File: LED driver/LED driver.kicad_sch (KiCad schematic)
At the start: 49 parts, among them J1 Conn_VCC, J2 Conn_LED, J3 Conn_UART, J4 Conn_01x10, P1 USB_C_Plug_USB2.0, Q1 IRFZ44NS, Q2 IRFZ44NS, Q3 IRFZ44NS, Q4 IRFZ44NS, Q5 IRFZ44NS, SW1 SW_Push, U1 ESP32-S2-WROVER-I, U2 MP2359

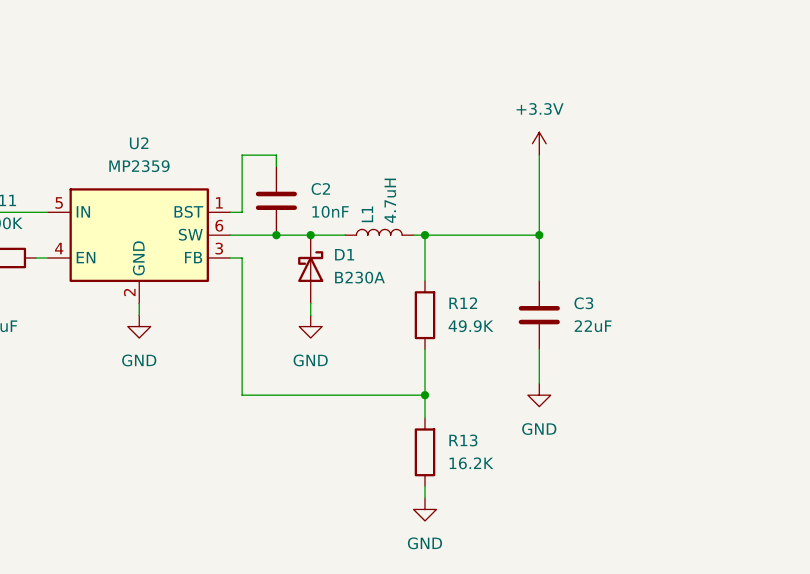
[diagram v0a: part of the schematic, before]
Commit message: update led driver, add turn signals
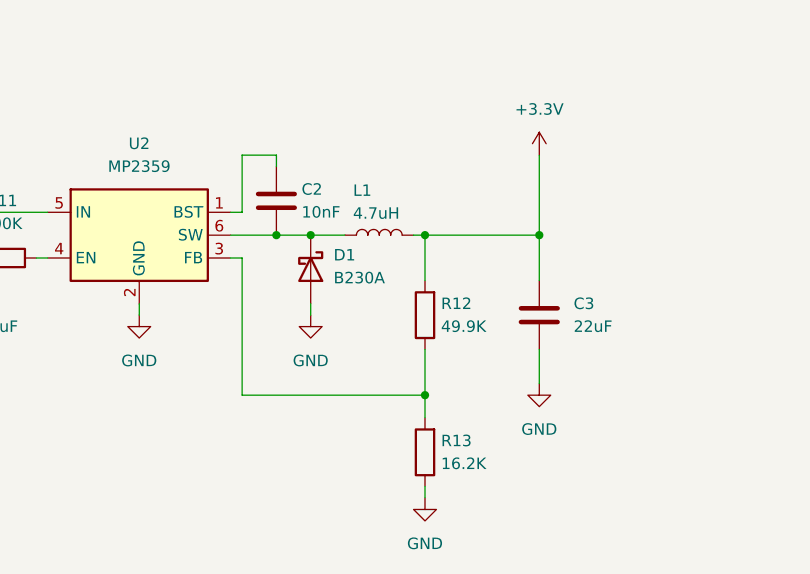
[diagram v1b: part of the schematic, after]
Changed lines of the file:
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@@
 		(on_board yes)
 		(dnp no)
-		(fields_autoplaced yes)
 		(property "Reference" "R11"
 			(at 25.4 156.21 90)
@@
 		(on_board yes)
 		(dnp no)
-		(fields_autoplaced yes)
 		(property "Reference" "R12"
-			(at 74.93 167.6399 0)
+			(at 74.168 167.6399 0)
 			(effects
 				(font
@@
 		)
 		(property "Value" "49.9K"
-			(at 74.93 170.1799 0)
+			(at 74.168 170.1799 0)
 			(effects
 				(font
@@
 		(on_board yes)
 		(dnp no)
-		(fields_autoplaced yes)
 		(property "Reference" "R13"
-			(at 74.93 182.8799 0)
+			(at 74.168 182.8799 0)
 			(effects
 				(font
@@
 		)
 		(property "Value" "16.2K"
-			(at 74.93 185.4199 0)
+			(at 74.168 185.4199 0)
 			(effects
 				(font
@@
 		(dnp no)
 		(property "Reference" "L1"
-			(at 66.0399 158.75 0)
+			(at 64.389 155.0669 90)
 			(effects
 				(font
 					(size 1.27 1.27)
 				)
-				(justify left)
+				(justify right)
 			)
 		)
 		(property "Value" "4.7uH"
-			(at 68.5799 158.75 0)
+			(at 64.389 157.6069 90)
 			(effects
 				(font
 					(size 1.27 1.27)
 				)
-				(justify left)
+				(justify right)
 			)
 		)
@@
 		(on_board yes)
 		(dnp no)
-		(fields_autoplaced yes)
 		(property "Reference" "C2"
-			(at 59.69 154.9399 0)
+			(at 58.674 154.9399 0)
 			(effects
 				(font
@@
 		)
 		(property "Value" "10nF"
-			(at 59.69 157.4799 0)
+			(at 58.674 157.4799 0)
 			(effects
 				(font

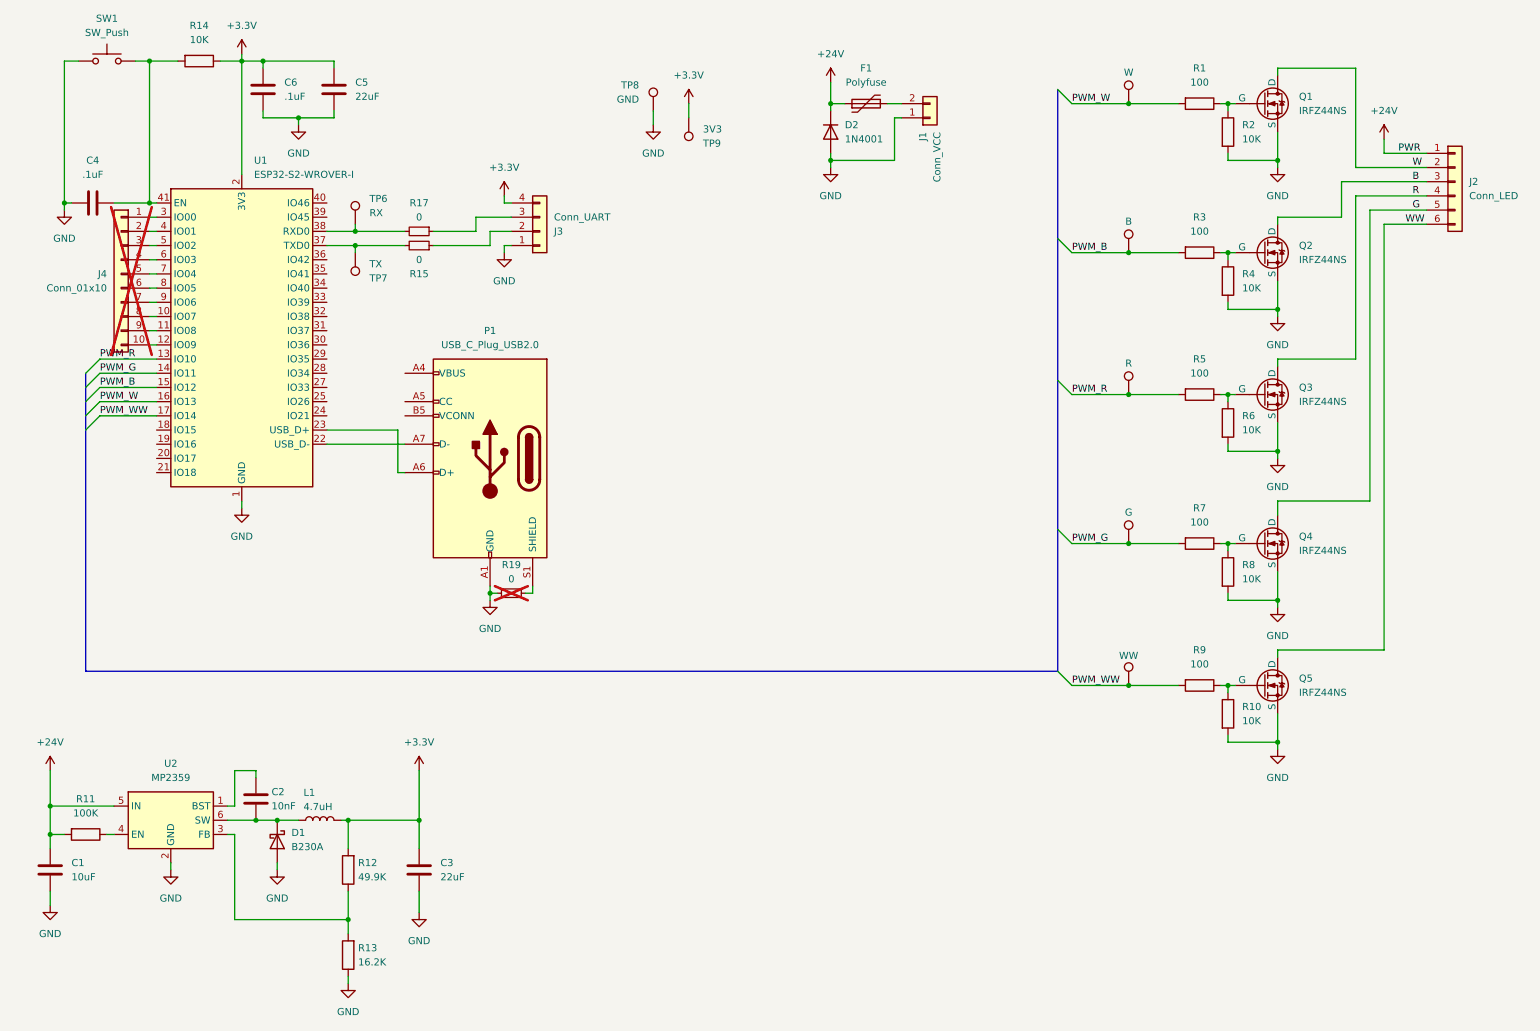
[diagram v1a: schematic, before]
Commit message: update LED driver
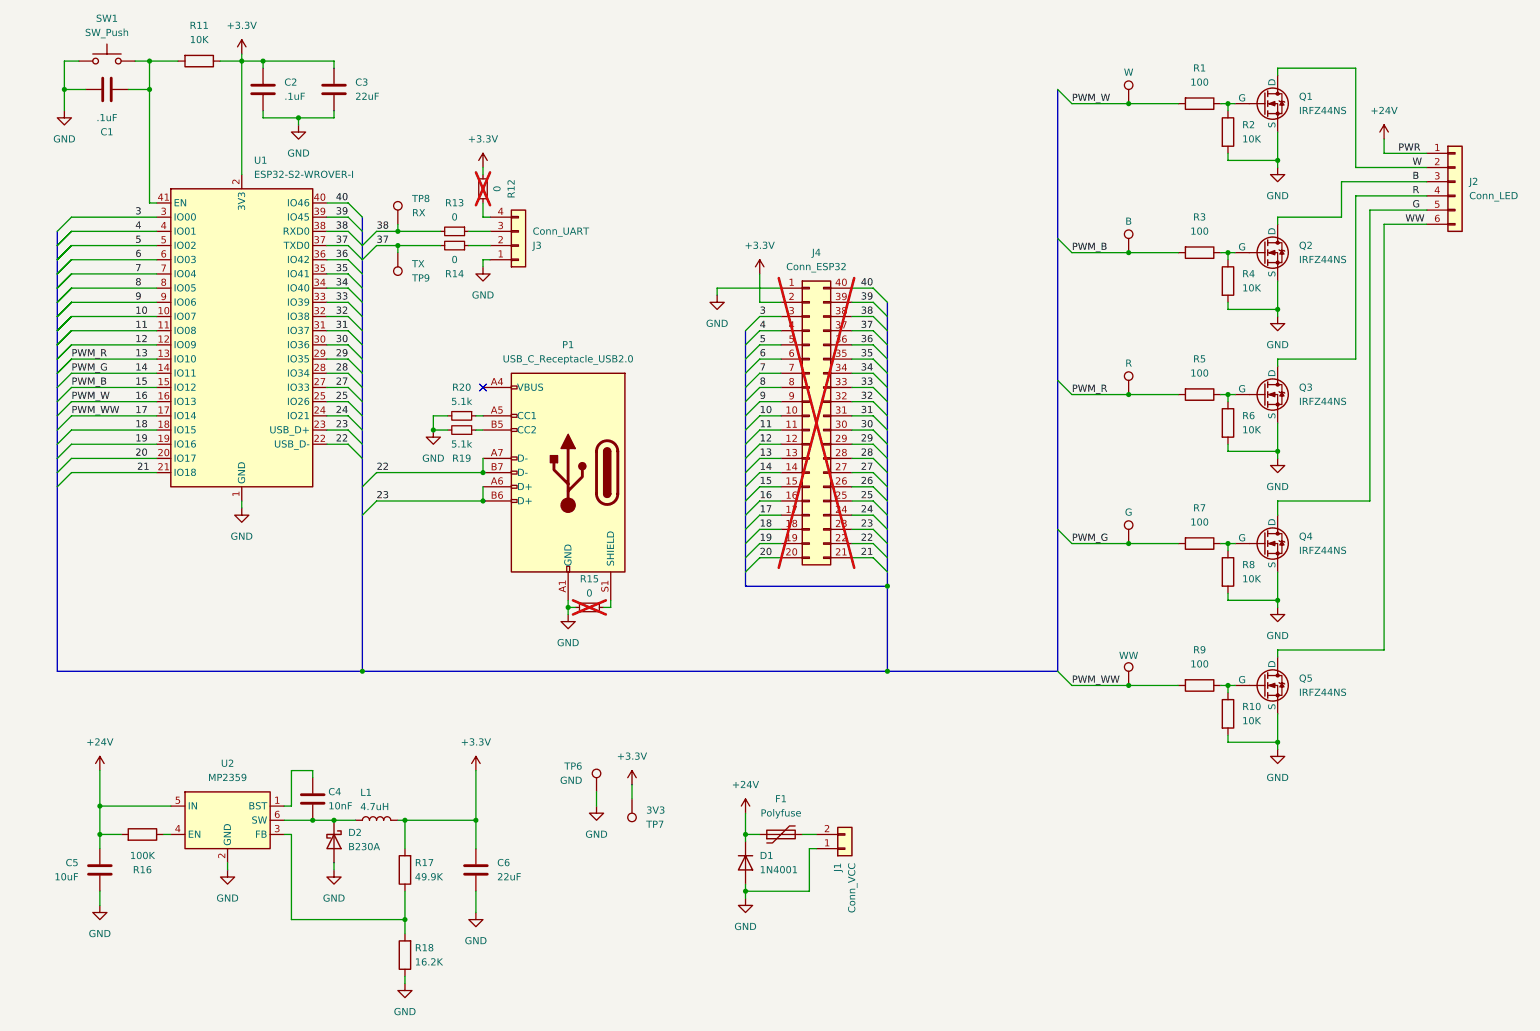
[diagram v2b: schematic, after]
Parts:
- removed J4: Conn_01x10, Connector_PinHeader_2.54mm:PinHeader_1x10_P2.54mm_Vertical, symbol Connector_Generic:Conn_01x10
- added J4: Conn_ESP32, Connector_PinSocket_2.54mm:PinSocket_2x20_P2.54mm_Vertical, symbol Connector_Generic:Conn_02x20_Counter_Clockwise
- added R12: 0, Resistor_SMD:R_0603_1608Metric_Pad0.98x0.95mm_HandSolder, symbol Device:R_Small
- added R19, R20: 5.1k, Resistor_SMD:R_0603_1608Metric_Pad0.98x0.95mm_HandSolder, symbol Device:R_Small
- P1: value USB_C_Plug_USB2.0 -> USB_C_Receptacle_USB2.0; footprint Connector_USB:USB_C_Receptacle_GCT_USB4105-xx-A_16P_TopMnt_Horizontal -> Connector_USB:USB_C_Receptacle_Amphenol_12401548E4-2A; symbol Connector:USB_C_Plug_USB2.0 -> Connector:USB_C_Receptacle_USB2.0_14P
- TP1, TP2, TP3, TP4, TP5: footprint TestPoint:TestPoint_Pad_D2.0mm -> TestPoint:TestPoint_Pad_D1.5mm
- TP6: renamed from TP8; footprint TestPoint:TestPoint_Pad_D2.0mm -> TestPoint:TestPoint_Pad_D1.5mm
- TP7: renamed from TP9; footprint TestPoint:TestPoint_Pad_D2.0mm -> TestPoint:TestPoint_Pad_D1.5mm
- TP8: renamed from TP6; footprint TestPoint:TestPoint_Pad_D2.0mm -> TestPoint:TestPoint_Pad_D1.5mm
- TP9: renamed from TP7; footprint TestPoint:TestPoint_Pad_D2.0mm -> TestPoint:TestPoint_Pad_D1.5mm
- renumbered C4 to C1, C6 to C2, C5 to C3, C2 to C4, C1 to C5, C3 to C6, D2 to D1, D1 to D2, R14 to R11, R17 to R13, R15 to R14, R19 to R15, R11 to R16, R12 to R17, R13 to R18
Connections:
- net +3.3V: now also J4.2 (Pin_2), R12.2; no longer J3.4 (Pin_4)
- net GND: now also J4.1 (Pin_1), R19.2, R20.2
- net 10: now reaches U1.10 (IO07)
- net 10: now also J4.10 (Pin_10)
- net 11: now reaches U1.11 (IO08)
- net 11: now also J4.11 (Pin_11)
- net 12: now reaches U1.12 (IO09)
- net 12: now also J4.12 (Pin_12)
- net 18: now reaches U1.18 (IO15)
- net 18: now also J4.18 (Pin_18)
- net 19: now reaches U1.19 (IO16)
- net 19: now also J4.19 (Pin_19)
- net 20: now reaches U1.20 (IO17)
- net 20: now also J4.20 (Pin_20)
- net 21: now reaches U1.21 (IO18)
- net 21: now also J4.21 (Pin_21)
- net 22: now reaches P1.A7 (D-), U1.22 (USB_D-)
- net 22: now also P1.B7 (D-), J4.22 (Pin_22)
- net 23: now reaches P1.A6 (D+), U1.23 (USB_D+)
- net 23: now also P1.B6 (D+), J4.23 (Pin_23)
- net 24: now reaches U1.24 (IO21)
- net 24: now also J4.24 (Pin_24)
- net 25: now reaches U1.25 (IO26)
- net 25: now also J4.25 (Pin_25)
- net 27: now reaches U1.27 (IO33)
- net 27: now also J4.27 (Pin_27)
- net 28: now reaches U1.28 (IO34)
- net 28: now also J4.28 (Pin_28)
- net 29: now reaches U1.29 (IO35)
- net 29: now also J4.29 (Pin_29)
- net 3: now reaches U1.3 (IO00)
- net 3: now also J4.3 (Pin_3)
- net 30: now reaches U1.30 (IO36)
- net 30: now also J4.30 (Pin_30)
- net 31: now reaches U1.31 (IO37)
- net 31: now also J4.31 (Pin_31)
- net 32: now reaches U1.32 (IO38)
- net 32: now also J4.32 (Pin_32)
- net 33: now reaches U1.33 (IO39)
- net 33: now also J4.33 (Pin_33)
- net 34: now reaches U1.34 (IO40)
- net 34: now also J4.34 (Pin_34)
- net 35: now reaches U1.35 (IO41)
- net 35: now also J4.35 (Pin_35)
- net 36: now reaches U1.36 (IO42)
- net 36: now also J4.36 (Pin_36)
- net 37: now reaches R14.2, TP9.1, U1.37 (TXD0)
- net 37: now also J4.37 (Pin_37)
- net 38: now reaches R13.2, TP8.1, U1.38 (RXD0)
- net 38: now also J4.38 (Pin_38)
- net 39: now reaches U1.39 (IO45)
- net 39: now also J4.39 (Pin_39)
- net 4: now reaches U1.4 (IO01)
- net 4: now also J4.4 (Pin_4)
- net 40: now reaches U1.40 (IO46)
- net 40: now also J4.40 (Pin_40)
- net 5: now reaches U1.5 (IO02)
- net 5: now also J4.5 (Pin_5)
- net 6: now reaches U1.6 (IO03)
- net 6: now also J4.6 (Pin_6)
- net 7: now reaches U1.7 (IO04)
- net 7: now also J4.7 (Pin_7)
- net 8: now reaches U1.8 (IO05)
- net 8: now also J4.8 (Pin_8)
- net 9: now reaches U1.9 (IO06)
- net 9: now also J4.9 (Pin_9)
- net at P1.A5 (CC1): now also R20.1
- net at P1.B5 (CC2): now also R19.1
- net PWM_B renamed 15
- net 15: now also J4.15 (Pin_15)
- net PWM_G renamed 14
- net 14: now also J4.14 (Pin_14)
- net PWM_R renamed 13
- net 13: now also J4.13 (Pin_13)
- net PWM_W renamed 16
- net 16: now also J4.16 (Pin_16)
- net PWM_WW renamed 17
- net 17: now also J4.17 (Pin_17)
- new net: J3.4 (Pin_4), R12.1
- new net 26: J4.26 (Pin_26)
- no-connect marks 0 -> 1
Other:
- moved on the sheet: C1, C4, C5, C6, D1, D2, F1, J1, J3, L1, R13, R14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

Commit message: update led driver
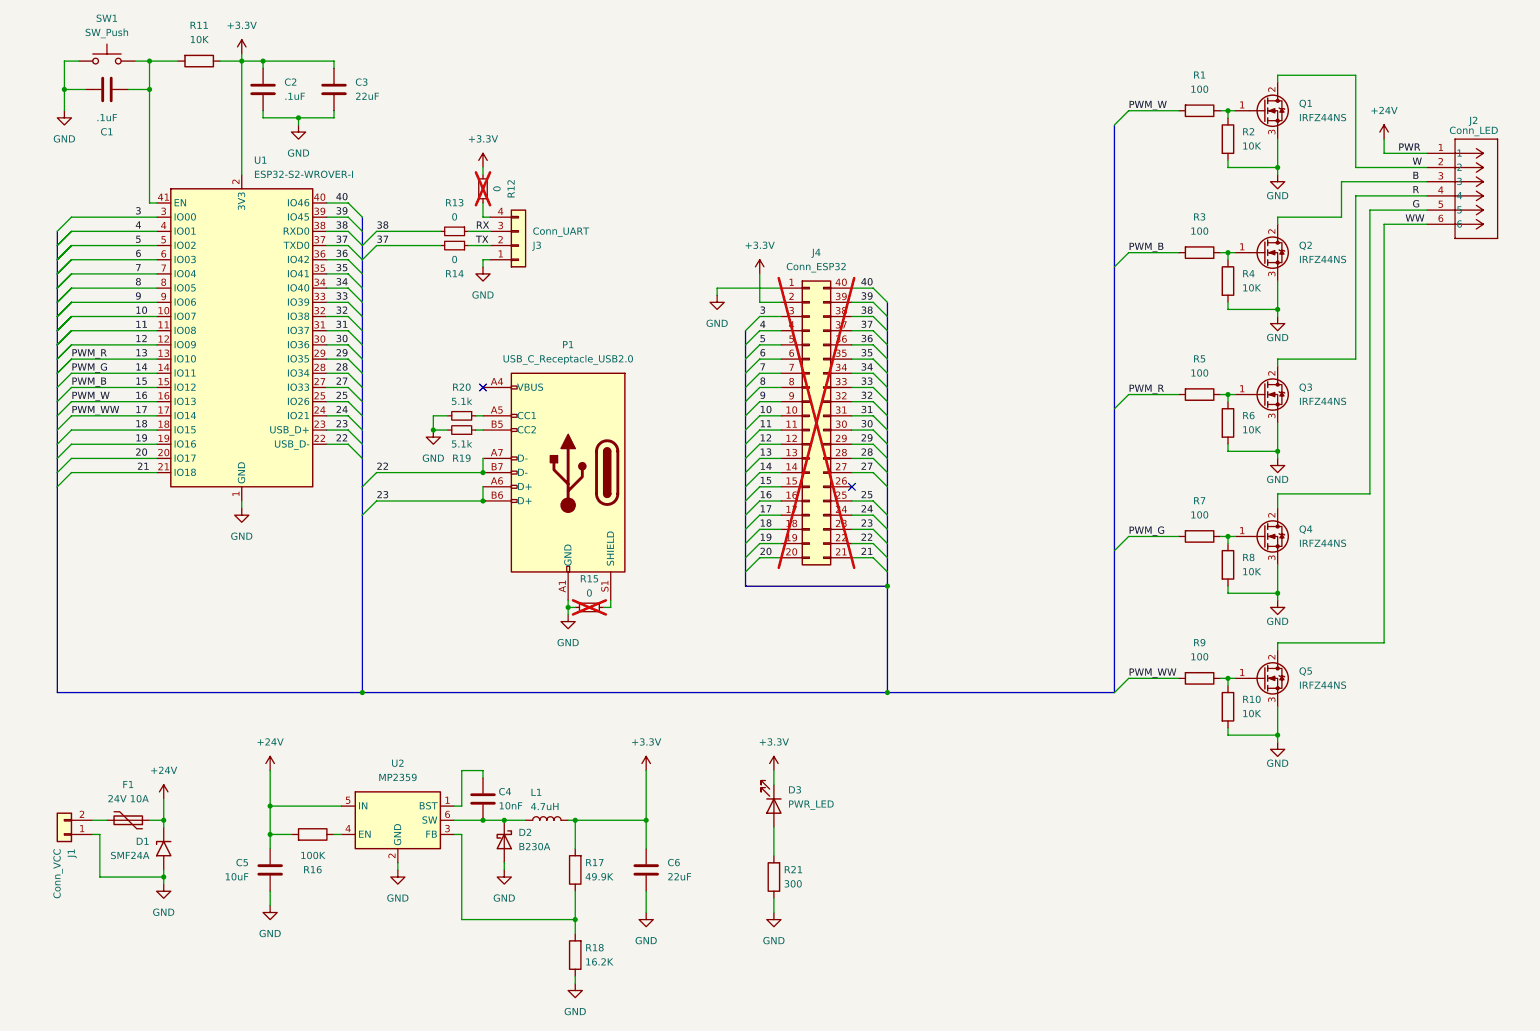
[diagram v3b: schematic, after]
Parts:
- removed TP1: W, TestPoint:TestPoint_Pad_D1.5mm, symbol Connector:TestPoint
- removed TP2: B, TestPoint:TestPoint_Pad_D1.5mm, symbol Connector:TestPoint
- removed TP3: R, TestPoint:TestPoint_Pad_D1.5mm, symbol Connector:TestPoint
- removed TP4: G, TestPoint:TestPoint_Pad_D1.5mm, symbol Connector:TestPoint
- removed TP5: WW, TestPoint:TestPoint_Pad_D1.5mm, symbol Connector:TestPoint
- removed TP6: GND, TestPoint:TestPoint_Pad_D1.5mm, symbol Connector:TestPoint
- removed TP7: 3V3, TestPoint:TestPoint_Pad_D1.5mm, symbol Connector:TestPoint
- removed TP8: RX, TestPoint:TestPoint_Pad_D1.5mm, symbol Connector:TestPoint
- removed TP9: TX, TestPoint:TestPoint_Pad_D1.5mm, symbol Connector:TestPoint
- added D3: PWR_LED, Diode_SMD:D_0603_1608Metric_Pad1.05x0.95mm_HandSolder, symbol Device:LED
- added R21: 300, Custom:R_0603_HandSolder_ValuePrinted, symbol Device:R
- C1, C2, C3, C4, C5, C6: footprint Capacitor_SMD:C_0603_1608Metric_Pad1.08x0.95mm_HandSolder -> Custom:C_0603_HandSolder_ValuePrinted
- D1: value 1N4001 -> SMF24A; footprint Diode_THT:D_DO-41_SOD81_P10.16mm_Horizontal -> Diode_SMD:D_SMF; symbol Diode:1N4001 -> Diode:SMF24A
- F1: value Polyfuse -> 24V 10A
- J2: footprint Connector_PinHeader_2.54mm:PinHeader_1x06_P2.54mm_Vertical -> CON_532540670_MOL; symbol Connector_Generic:Conn_01x06 -> 2024-04-03_06-42-17:532540670
- P1: footprint Connector_USB:USB_C_Receptacle_Amphenol_12401548E4-2A -> Connector_USB:USB_C_Receptacle_GCT_USB4105-xx-A_16P_TopMnt_Horizontal
- R1, R10, R11, R16, R17, R18, R19, R2, R20, R3, R4, R5, R6, R7, R8, R9: footprint Resistor_SMD:R_0603_1608Metric_Pad0.98x0.95mm_HandSolder -> Custom:R_0603_HandSolder_ValuePrinted
- U1: footprint RF_Module:ESP32-S2-WROVER -> Custom:ESP32-S2-WROVER
- U2: footprint Package_TO_SOT_SMD:TSOT-23-6_HandSoldering -> Package_TO_SOT_SMD:TSOT-23-6
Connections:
- net +3.3V: now also D3.1 (K)
- net GND: now also R21.1
- net RX: now reaches J3.3 (Pin_3), R13.1
- net TX: now reaches J3.2 (Pin_2), R14.1
- net 26: no longer names the net of J4.26 (Pin_26)
- new net: D3.2 (A), R21.2
- no-connect marks 1 -> 2
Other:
- moved on the sheet: C4, C5, C6, D2, F1, J1, L1, Q1, Q4, Q5, R1, R10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

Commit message: led driver
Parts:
- removed J4: Conn_ESP32, Connector_PinSocket_2.54mm:PinSocket_2x20_P2.54mm_Vertical, symbol Connector_Generic:Conn_02x20_Counter_Clockwise
- removed P1: USB_C_Receptacle_USB2.0, Connector_USB:USB_C_Receptacle_GCT_USB4105-xx-A_16P_TopMnt_Horizontal, symbol Connector:USB_C_Receptacle_USB2.0_14P
- removed R15: 0, Resistor_SMD:R_0603_1608Metric_Pad0.98x0.95mm_HandSolder, symbol Device:R_Small
- removed R19, R20: 5.1k, Custom:R_0603_HandSolder_ValuePrinted, symbol Device:R_Small
- added J4: Conn_Boot_Mode, Connector_PinHeader_2.54mm:PinHeader_1x02_P2.54mm_Vertical, symbol Connector_Generic:Conn_01x02
- added J5: Conn_Aux, Connector_PinSocket_2.54mm:PinSocket_2x03_P2.54mm_Vertical, symbol Connector_Generic:Conn_02x03_Odd_Even
- added R15, R22: 10K, Custom:R_0603_HandSolder_ValuePrinted, symbol Device:R
- C2: value .1uF -> 0.1uF
- C3: value 22uF -> 10uF
- J2: footprint CON_532540670_MOL -> footprints:CON_532540670_MOL
- U1: value ESP32-S2-WROVER-I -> ESP32-C3-WROOM-02; footprint Custom:ESP32-S2-WROVER -> RF_Module:ESP32-C3-WROOM-02; symbol RF_Module:ESP32-S2-WROVER-I -> Custom:ESP32-C3-WROOM-02
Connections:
- net 19 is gone; now on net GND: U1.19 (GND)
- net 9 is gone; now on net GND: U1.9 (GND)
- net +3.3V: now also C2.2, C3.2, U1.1 (VDD), J5.2 (Pin_2), R15.1, R22.1; no longer C2.1, C3.1, U1.2 (3V3)
- net GND: now also C2.1, C3.1, J4.1 (Pin_1), J5.1 (Pin_1); no longer C2.2, C3.2, U1.1 (GND), U1.26 (GND), U1.42 (GND), U1.43 (GND)
- net at C1.2, R11.2, SW1.2: now also U1.2 (EN); no longer U1.41 (EN)
- net 10: no longer names the net of U1.10 (IO10)
- net 11: no longer names the net of U1.11 (RXD)
- net 11: now also R13.2
- net 12: no longer names the net of U1.12 (TXD)
- net 12: now also R14.2
- net 13: no longer names the net of U1.13 (IO18)
- net 13: no longer R5.2
- net 14 renamed PWM_G
- net PWM_G: now also U1.17 (IO1); no longer U1.14 (IO11)
- net 15 renamed PWM_B
- net PWM_B: now also U1.16 (IO2); no longer U1.15 (IO12)
- net 16 renamed PWM_W
- net PWM_W: now also U1.15 (IO3); no longer U1.16 (IO13)
- net 17 renamed PWM_WW
- net PWM_WW: now also U1.14 (IO19); no longer U1.17 (IO14)
- net 18 renamed PWM_R
- net PWM_R: now also R5.2
- removed net 20: U1.20 (IO17)
- removed net 21: U1.21 (IO18)
- removed net 22: U1.22 (USB_D-)
- removed net 23: U1.23 (USB_D+)
- removed net 24: U1.24 (IO21)
- removed net 25: U1.25 (IO26)
- removed net 27: U1.27 (IO33)
- removed net 28: U1.28 (IO34)
- removed net 29: U1.29 (IO35)
- net 3 renamed IO4
- net IO4: now also J5.3 (Pin_3)
- removed net 30: U1.30 (IO36)
- removed net 31: U1.31 (IO37)
- removed net 32: U1.32 (IO38)
- removed net 33: U1.33 (IO39)
- removed net 34: U1.34 (IO40)
- removed net 35: U1.35 (IO41)
- removed net 36: U1.36 (IO42)
- removed net 37: R14.2, U1.37 (TXD0)
- removed net 38: R13.2, U1.38 (RXD0)
- removed net 39: U1.39 (IO45)
- net 4 renamed IO5
- net IO5: now also J5.4 (Pin_4)
- removed net 40: U1.40 (IO46)
- net 5 renamed IO6
- net IO6: now also J5.5 (Pin_5)
- net 6 renamed IO7
- net IO7: now also J5.6 (Pin_6)
- net 7: no longer names the net of U1.7 (IO8)
- net 7: now also R22.2
- net 8: no longer names the net of U1.8 (IO9)
- net 8: now also J4.2 (Pin_2)
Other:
- moved on the sheet: C1, C3, J3, R11, R12, R13, R14, SW1
